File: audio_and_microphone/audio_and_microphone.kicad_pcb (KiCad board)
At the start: 2 copper layers, 15 parts

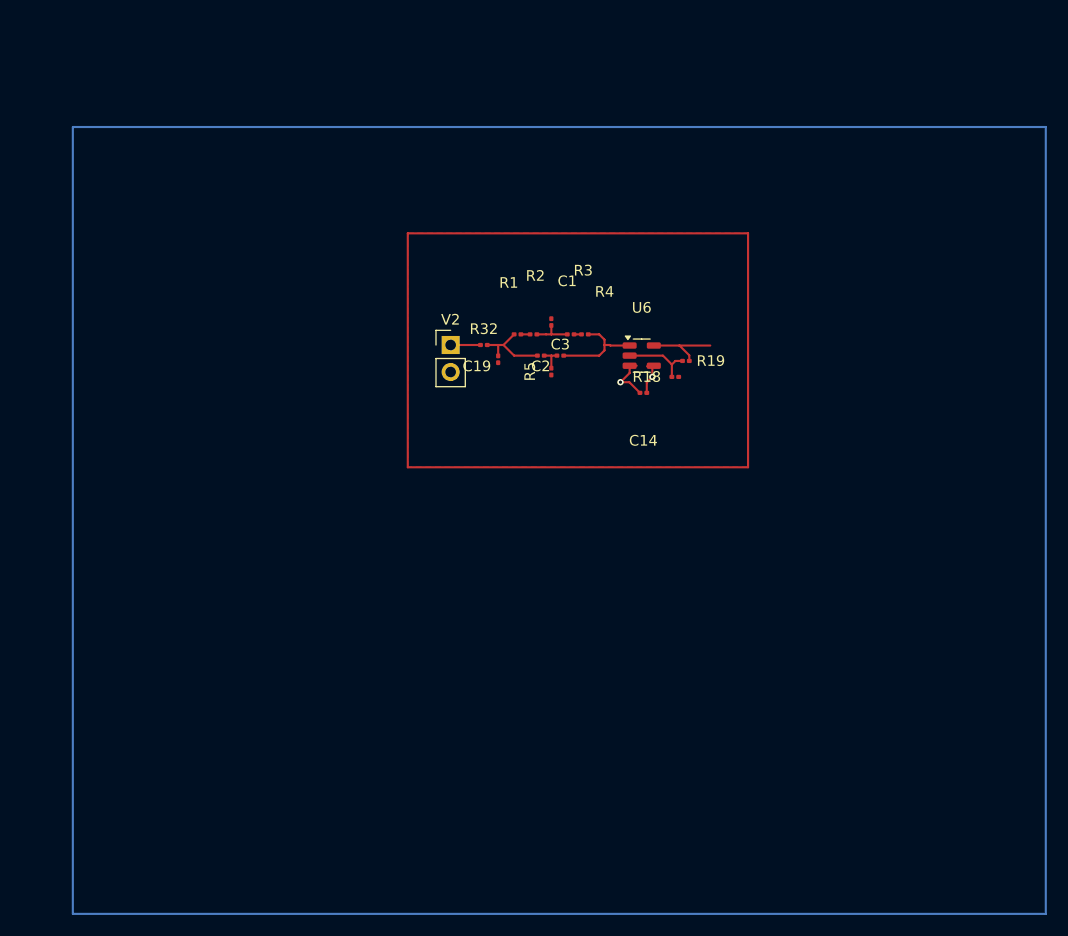
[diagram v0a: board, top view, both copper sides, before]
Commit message: updated pcb with components and locked pin holders NON THRU
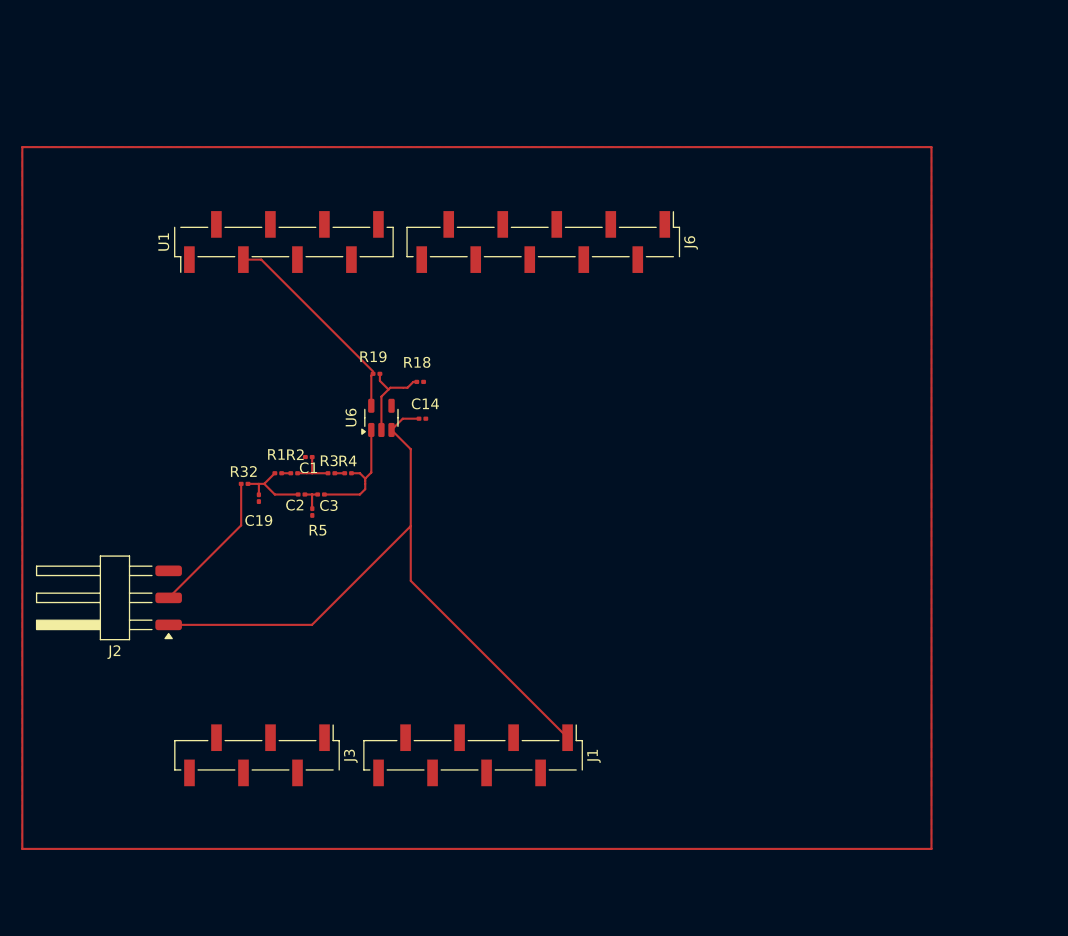
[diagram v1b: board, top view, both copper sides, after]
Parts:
- removed V2: VPWL, Connector_PinHeader_2.54mm:PinHeader_1x02_P2.54mm_Vertical
- added J1: Conn_01x08_MountingPin, Connector_PinHeader_2.54mm:PinHeader_1x08_P2.54mm_Vertical_SMD_Pin1Left, F.Cu at (124.6, 140.6)
- added J2: Conn_01x03_MountingPin, Connector_Harwin:Harwin_M20-89003xx_1x03_P2.54mm_Horizontal, F.Cu at (90.5, 125.8)
- added J3: Conn_01x06_MountingPin, Connector_PinHeader_2.54mm:PinHeader_1x06_P2.54mm_Vertical_SMD_Pin1Left, F.Cu at (104.3, 140.6)
- added J6: Conn_01x10_MountingPin, Connector_PinHeader_2.54mm:PinHeader_1x10_P2.54mm_Vertical_SMD_Pin1Left, F.Cu at (131.2, 92.3)
- added U1: nRF52833_QDxx, Connector_PinHeader_2.54mm:PinHeader_1x08_P2.54mm_Vertical_SMD_Pin1Left, F.Cu at (106.8, 92.3)
- moved R19 29.1 mm to (115.6, 104.7), turned to 0 degrees
- moved C1 26.1 mm to (109.2, 112.5), turned to 180 degrees
- moved R5 26.1 mm to (109.5, 117.7)
- moved C19 26.0 mm to (104.5, 116.4)
- moved C2 26.0 mm to (108.5, 116.1)
- moved C3 26.0 mm to (110.3, 116.1)
- moved R1 26.0 mm to (106.3, 114.1)
- moved R2 26.0 mm to (107.8, 114.1)
- moved R3 26.0 mm to (111.3, 114.1)
- moved R32 26.0 mm to (103.2, 115.1)
- moved R4 25.8 mm to (112.9, 114.1)
- moved U6 25.2 mm to (116.0, 108.9), turned to 90 degrees
- moved R18 24.0 mm to (119.7, 105.5)
- moved C14 20.9 mm to (119.9, 108.9)
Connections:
- R32 pad 2: Net-(R32-Pad2) -> +3V3
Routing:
- net +3V3: track 4.82 -> 65.4 mm, vias 1 -> 0
- net (no net): track 0.00 -> 13.5 mm
- net /ENV_OUT: track 7.15 -> 19.6 mm
- net Net-(R32-Pad2): track 3.51 -> 0.00 mm
- net GND: track 3.48 -> 0.27 mm, vias 1 -> 0
- net Net-(U6-+): track 9.16 -> 11.3 mm
- net Net-(U6--): track 6.62 -> 8.76 mm
- net Net-(C1-Pad1): track 3.70 -> 4.39 mm

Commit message: updated pcb board with switch mechanisms for old vs new filters and tht pin holes
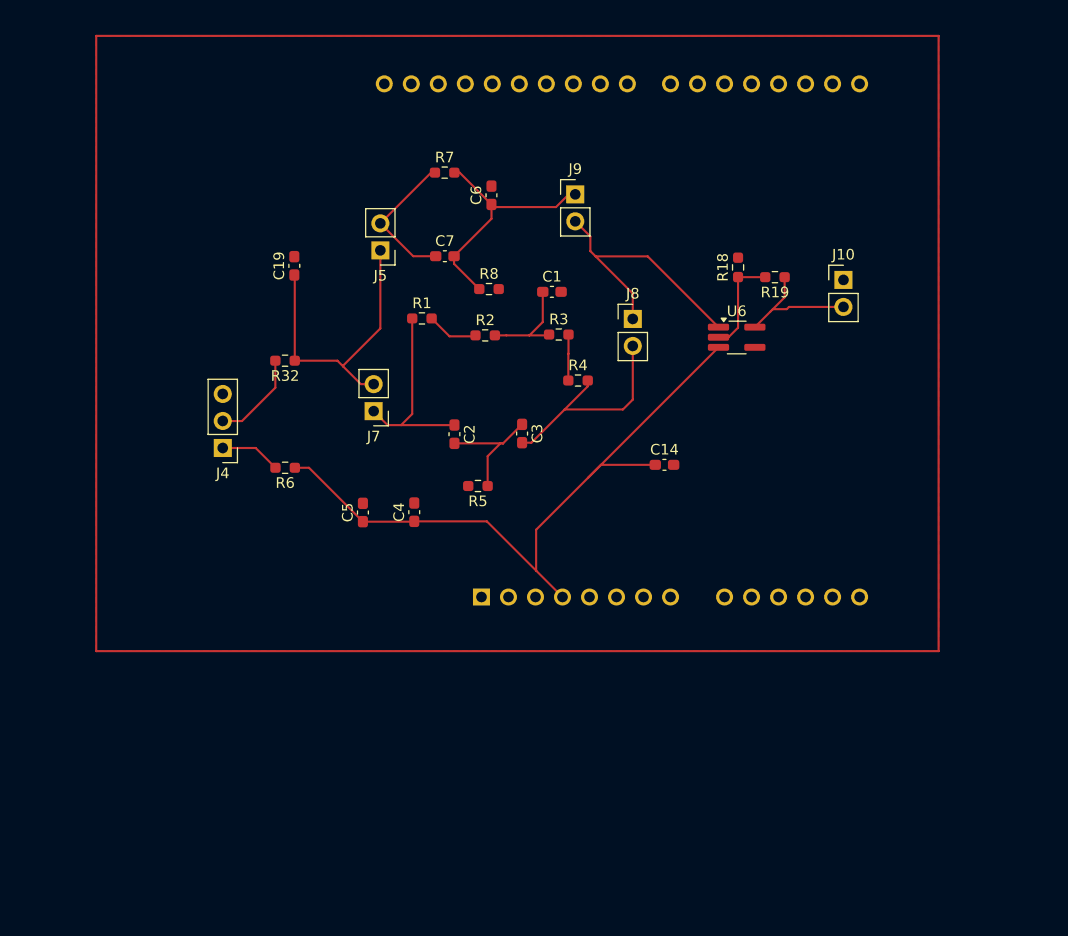
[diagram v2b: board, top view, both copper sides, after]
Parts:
- removed J1: Conn_01x08_MountingPin, Connector_PinHeader_2.54mm:PinHeader_1x08_P2.54mm_Vertical_SMD_Pin1Left
- removed J2: Conn_01x03_MountingPin, Connector_Harwin:Harwin_M20-89003xx_1x03_P2.54mm_Horizontal
- removed J3: Conn_01x06_MountingPin, Connector_PinHeader_2.54mm:PinHeader_1x06_P2.54mm_Vertical_SMD_Pin1Left
- removed J6: Conn_01x10_MountingPin, Connector_PinHeader_2.54mm:PinHeader_1x10_P2.54mm_Vertical_SMD_Pin1Left
- removed U1: nRF52833_QDxx, Connector_PinHeader_2.54mm:PinHeader_1x08_P2.54mm_Vertical_SMD_Pin1Left
- added A1: Arduino_UNO_R3, Module:Arduino_UNO_R3, B.Cu at (125.4, 125.7)
- added C4: C, Capacitor_SMD:C_0603_1608Metric_Pad1.08x0.95mm_HandSolder, F.Cu at (119.1, 117.7)
- added C5: C, Capacitor_SMD:C_0603_1608Metric_Pad1.08x0.95mm_HandSolder, F.Cu at (114.3, 117.8)
- added C6: 0.2u, Capacitor_SMD:C_0603_1608Metric_Pad1.08x0.95mm_HandSolder, F.Cu at (126.4, 87.9)
- added C7: 0.2u, Capacitor_SMD:C_0603_1608Metric_Pad1.08x0.95mm_HandSolder, F.Cu at (122.0, 93.7)
- added J10: Conn_01x02_Pin, Connector_PinHeader_2.54mm:PinHeader_1x02_P2.54mm_Vertical, F.Cu at (159.5, 95.9)
- added J4: Conn_01x03_Pin, Connector_PinHeader_2.54mm:PinHeader_1x03_P2.54mm_Vertical, F.Cu at (101.1, 111.7)
- added J5: Conn_01x02, Connector_PinHeader_2.54mm:PinHeader_1x02_P2.54mm_Vertical, F.Cu at (115.9, 93.1)
- added J7: Conn_01x02, Connector_PinHeader_2.54mm:PinHeader_1x02_P2.54mm_Vertical, F.Cu at (115.3, 108.2)
- added J8: Conn_01x02, Connector_PinHeader_2.54mm:PinHeader_1x02_P2.54mm_Vertical, F.Cu at (139.7, 99.5)
- added J9: Conn_01x02, Connector_PinHeader_2.54mm:PinHeader_1x02_P2.54mm_Vertical, F.Cu at (134.2, 87.8)
- added R6: 6.2K, Resistor_SMD:R_0603_1608Metric_Pad0.98x0.95mm_HandSolder, F.Cu at (107.0, 113.5)
- added R7: 150k, Resistor_SMD:R_0603_1608Metric_Pad0.98x0.95mm_HandSolder, F.Cu at (122.0, 85.8)
- added R8: 10k, Resistor_SMD:R_0603_1608Metric_Pad0.98x0.95mm_HandSolder, F.Cu at (126.1, 96.7)
- C1, C14, C19, C2, C3: footprint Capacitor_SMD:C_0201_0603Metric -> Capacitor_SMD:C_0603_1608Metric_Pad1.08x0.95mm_HandSolder
- R1, R18, R19, R2, R3, R32, R4, R5: footprint Resistor_SMD:R_0201_0603Metric -> Resistor_SMD:R_0603_1608Metric_Pad0.98x0.95mm_HandSolder
- U6: footprint Package_TO_SOT_SMD:SOT-23-5 -> Package_TO_SOT_SMD:TSOT-23-5_HandSoldering
- moved R19 38.6 mm to (153.0, 95.6), turned to 180 degrees
- moved U6 34.3 mm to (149.4, 101.3), turned to 0 degrees
- moved R18 31.8 mm to (149.6, 94.7), turned to 90 degrees
- moved C1 27.6 mm to (132.1, 97.0), turned to 0 degrees
- moved R3 25.0 mm to (132.7, 101.0)
- moved R4 23.3 mm to (134.5, 105.3)
- moved C14 23.2 mm to (142.6, 113.3)
- moved R2 22.2 mm to (125.8, 101.1)
- moved C19 22.1 mm to (107.8, 94.6), turned to 90 degrees
- moved R1 19.9 mm to (119.8, 99.5)
- moved C3 19.8 mm to (129.2, 110.3), turned to -90 degrees
- moved R5 15.8 mm to (125.1, 115.3), turned to 180 degrees
- moved C2 15.5 mm to (122.9, 110.4), turned to -90 degrees
- moved R32 12.2 mm to (107.0, 103.5)
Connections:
- net /ENV_OUT renamed ENV_OUT
- C19 pad 1: Net-(C19-Pad1) -> Net-(J5-Pin_1)
- C2 pad 1: Net-(C19-Pad1) -> Net-(J7-Pin_1)
- C3 pad 2: Net-(U6-+) -> Net-(J8-Pin_2)
- R1 pad 1: Net-(C19-Pad1) -> Net-(J7-Pin_1)
- R32 pad 1: Net-(C19-Pad1) -> Net-(J5-Pin_1)
- R32 pad 2: +3V3 -> Net-(J4-Pin_2)
- R4 pad 2: Net-(U6-+) -> Net-(J8-Pin_2)
- U6 pad 1: Net-(U6-+) -> Net-(J8-Pin_1)
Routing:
- net +3V3: track 65.4 -> 0.00 mm
- net +3.3V: track 0.00 -> 65.2 mm
- net Net-(J5-Pin_1): track 0.00 -> 28.8 mm
- net Net-(J8-Pin_1): track 0.00 -> 25.7 mm
- net Net-(J9-Pin_1): track 0.00 -> 23.6 mm
- net Net-(J8-Pin_2): track 0.00 -> 20.8 mm
- net Net-(J7-Pin_1): track 0.00 -> 18.6 mm
- net Net-(J5-Pin_2): track 0.00 -> 13.6 mm
- net (no net): track 13.5 -> 0.00 mm
- net Net-(U6-+): track 11.3 -> 0.00 mm
- net Net-(C2-Pad2): track 2.37 -> 11.6 mm
- net Net-(J4-Pin_2): track 0.00 -> 8.79 mm
- net Net-(C19-Pad1): track 7.57 -> 0.00 mm
- net ENV_OUT: track 19.6 -> 12.6 mm
- net Net-(J4-Pin_1): track 0.00 -> 5.74 mm
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
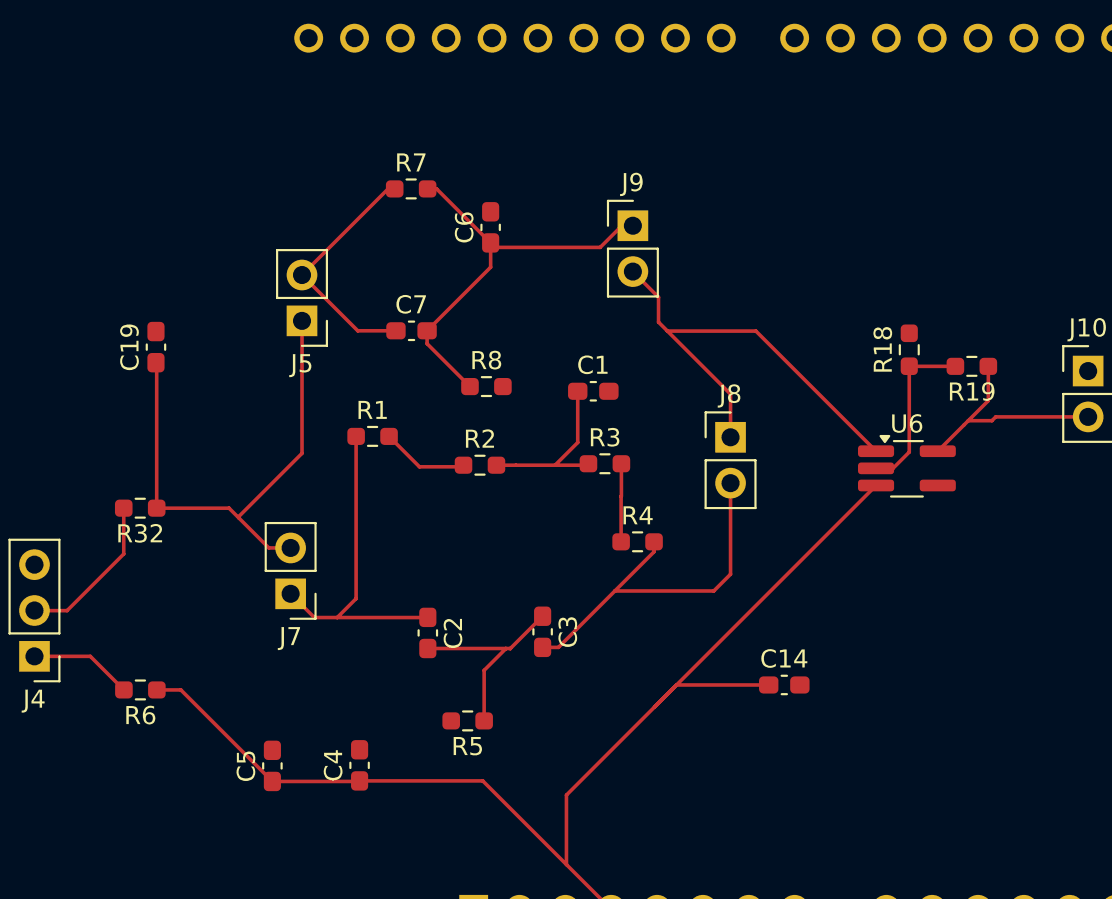
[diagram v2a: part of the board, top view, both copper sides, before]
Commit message: completed microphone circuit and updated the parts to match altium, ready for mill
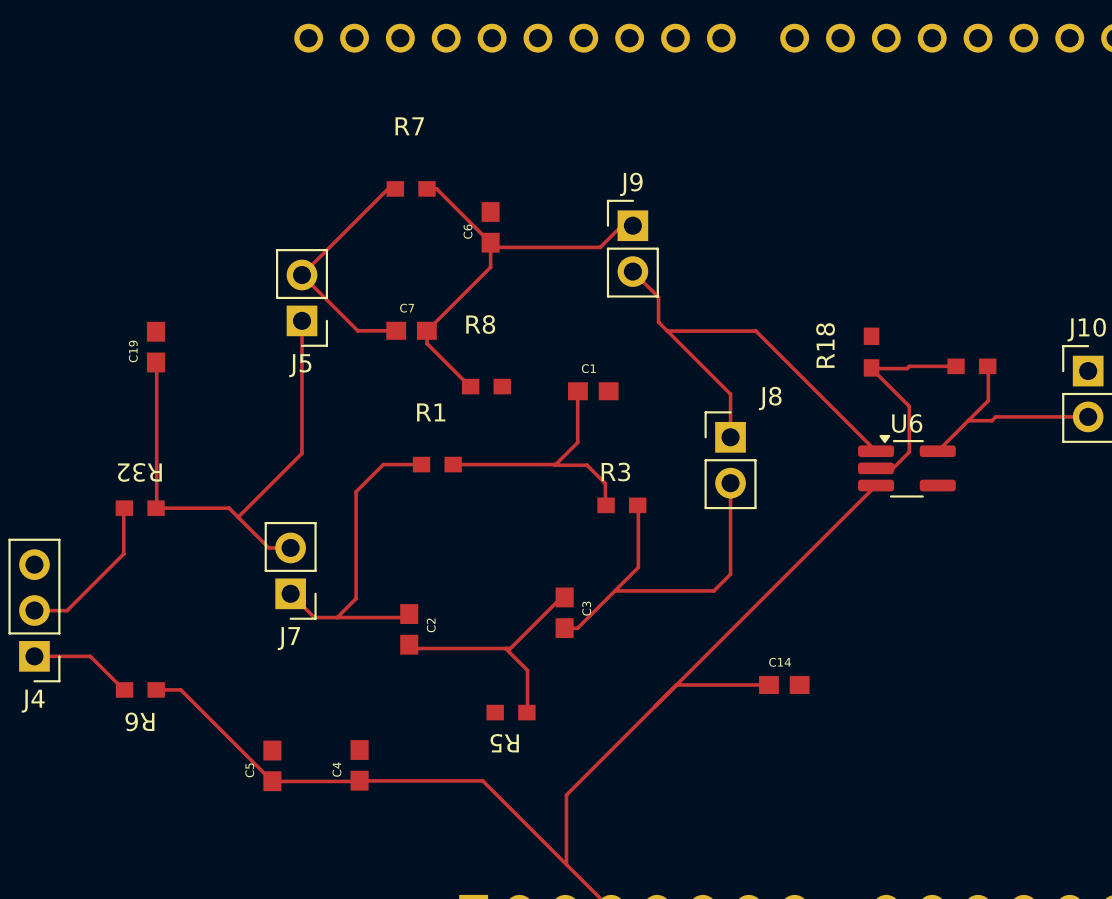
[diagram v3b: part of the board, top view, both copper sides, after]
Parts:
- removed R2, R4: 22k, Resistor_SMD:R_0603_1608Metric_Pad0.98x0.95mm_HandSolder
- C1, C14, C19, C2, C3, C4, C5, C6, C7: footprint Capacitor_SMD:C_0603_1608Metric_Pad1.08x0.95mm_HandSolder -> C0603C104K5RACTU:CAPC1608X90
- R1, R3: value 4.7k -> 26.7k; footprint Resistor_SMD:R_0603_1608Metric_Pad0.98x0.95mm_HandSolder -> Resistor1.60x0.80:RC0603N_YAG-M
- R18, R19, R32, R5, R6, R7, R8: footprint Resistor_SMD:R_0603_1608Metric_Pad0.98x0.95mm_HandSolder -> Resistor1.60x0.80:RC0603N_YAG-M
- moved R1 3.91 mm to (123.4, 101.1)
- moved R3 2.49 mm to (133.6, 103.3)
- moved R5 2.45 mm to (127.5, 114.8)
- moved R18 2.09 mm to (147.5, 94.8)
- moved C3 1.61 mm to (130.5, 109.3)
- moved C2 1.05 mm to (121.9, 110.2)
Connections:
- A1 pad 29: GND -> unconnected-(A1-GND-Pad29)
- A1 pad 6: GND -> unconnected-(A1-GND-Pad6)
- A1 pad 7: GND -> unconnected-(A1-GND-Pad7)
- R1 pad 2: Net-(R1-Pad2) -> Net-(C1-Pad1)
- R3 pad 2: Net-(R3-Pad2) -> Net-(J8-Pin_2)
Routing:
- net Net-(R1-Pad2): track 4.86 -> 0.00 mm
- net Net-(C1-Pad1): track 9.80 -> 14.7 mm
- net Net-(R3-Pad2): track 4.33 -> 0.00 mm
- net Net-(U6--): track 9.53 -> 12.4 mm
- net Net-(C2-Pad2): track 11.6 -> 13.9 mm

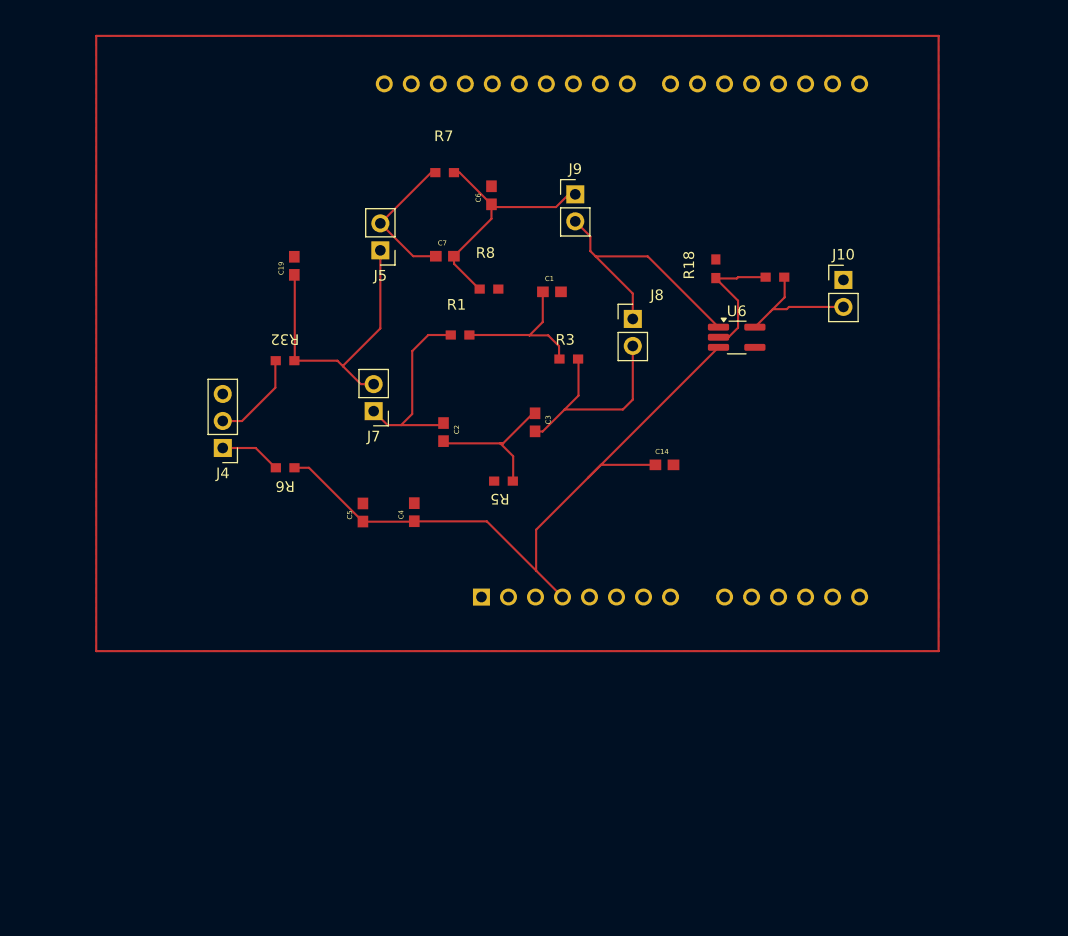
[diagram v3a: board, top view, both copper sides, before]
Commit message: updated pcb with two sides and back side with voltage
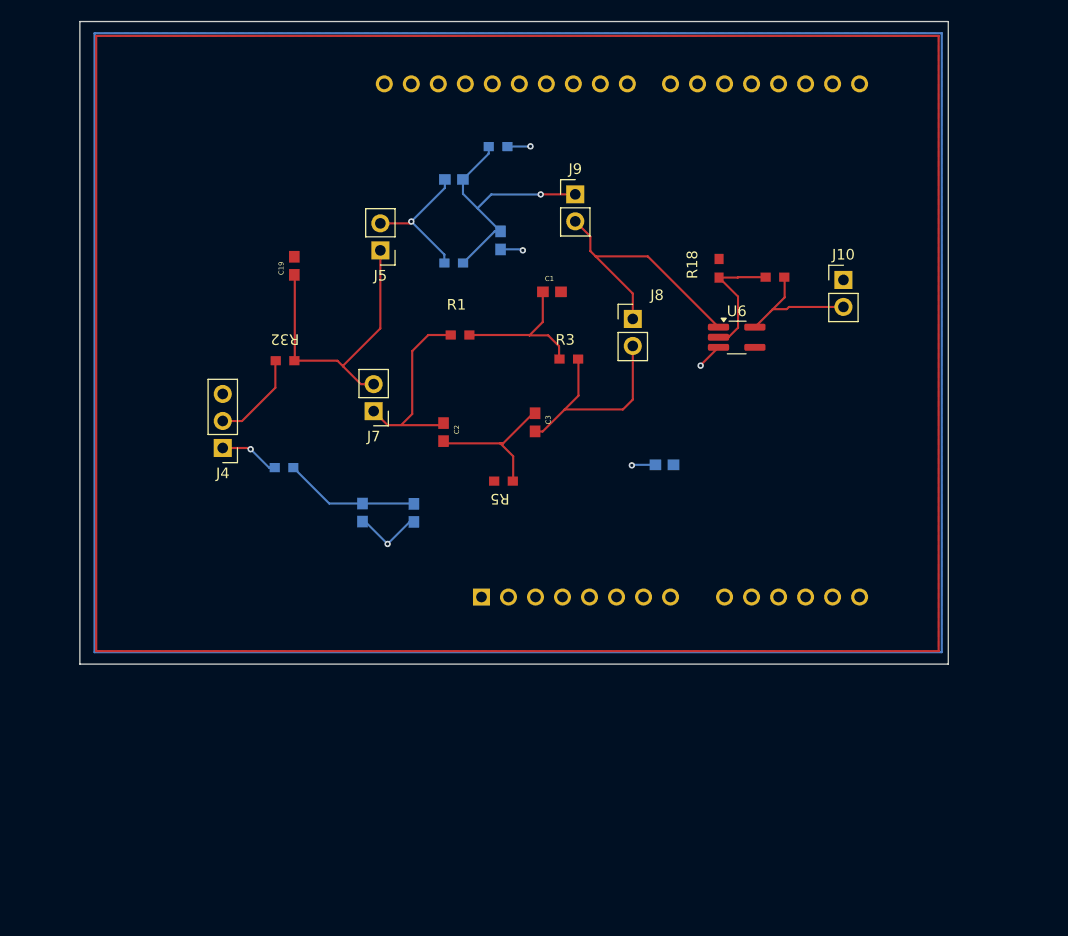
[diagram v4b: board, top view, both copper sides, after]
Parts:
- C14, C4, C5, C6, C7, R6, R7, R8: moved to B.Cu
- moved R8 13.4 mm to (127.0, 83.3)
- moved R7 8.54 mm to (122.8, 94.3)
- moved C7 7.27 mm to (122.8, 86.4)
- moved C6 4.32 mm to (127.2, 92.2), turned to -90 degrees
- moved R18 0.30 mm to (147.8, 94.8)
- moved R6 0.11 mm to (106.9, 113.5)
- moved C4 0.08 mm to (119.1, 117.8), turned to -90 degrees
- turned C5 to -90 degrees
- turned C14 to 180 degrees
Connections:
- A1 pad 4: unconnected-(A1-3V3-Pad4) -> +3.3V
- C14 pad 1: +3V3 -> +3.3V
- U6 pad 3: +3V3 -> +3.3V
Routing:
- net +3.3V: track 65.2 -> 15.2 mm, vias 0 -> 1
- net GND: track 0.00 -> 13.1 mm, vias 0 -> 4
- net Net-(J9-Pin_1): track 23.6 -> 25.3 mm, vias 0 -> 1
- net Net-(J5-Pin_2): track 13.6 -> 13.4 mm, vias 0 -> 1
- net Net-(J4-Pin_1): track 5.74 -> 5.66 mm, vias 0 -> 1
- added copper zone on B.Cu, net +3.3V
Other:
- board outline added: 81.7 x 60.4 mm
